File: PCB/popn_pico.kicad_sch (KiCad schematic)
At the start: 35 parts, among them SW1 KAN4542-0701C, SW2 KAN4542-0701C, U1 Pico

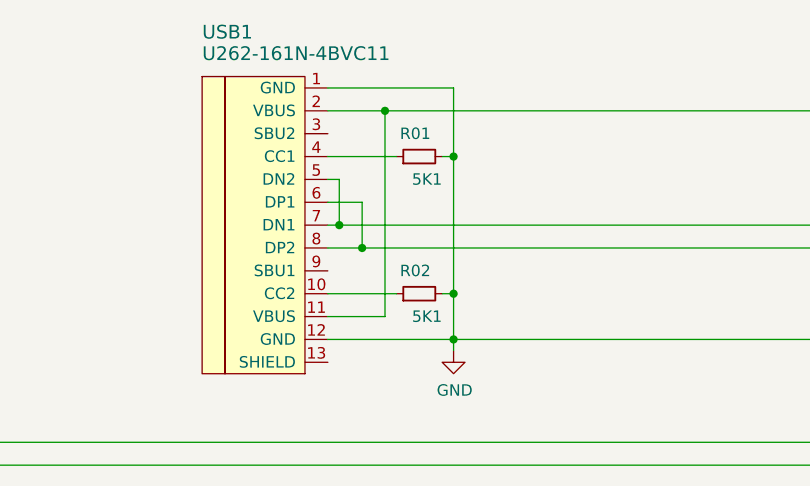
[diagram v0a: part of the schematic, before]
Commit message: Update PCB with libs and 3d models
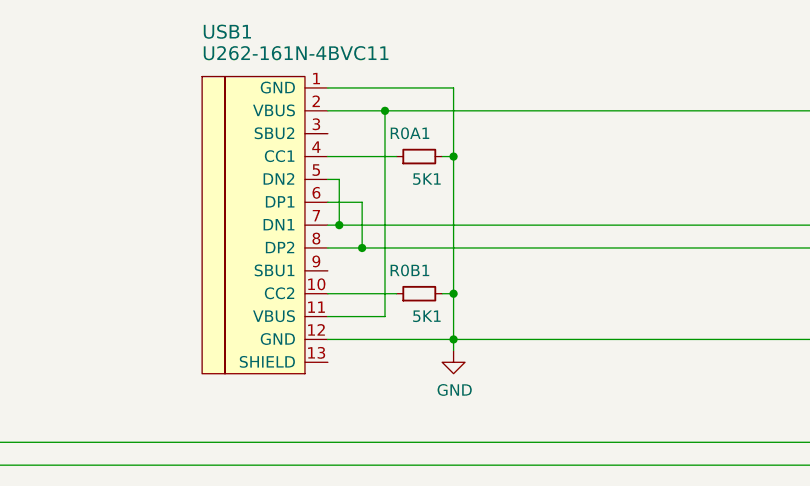
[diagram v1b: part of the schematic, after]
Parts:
- renumbered R01 to R0A1, R02 to R0B1
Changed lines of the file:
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@@
   (junction (at 199.39 142.24) (diameter 0) (color 0 0 0 0)
   )
+  (junction (at 259.08 106.68) (diameter 0) (color 0 0 0 0)
+  )
+  (junction (at 259.08 49.53) (diameter 0) (color 0 0 0 0)
+  )
+  (junction (at 95.25 180.34) (diameter 0) (color 0 0 0 0)
+  )
+  (junction (at 99.06 27.94) (diameter 0) (color 0 0 0 0)
+  )
+  (junction (at 262.89 74.93) (diameter 0) (color 0 0 0 0)
+  )
+  (junction (at 106.68 53.34) (diameter 0) (color 0 0 0 0)
+  )
+  (junction (at 262.89 109.22) (diameter 0) (color 0 0 0 0)
+  )
+  (junction (at 26.67 180.34) (diameter 0) (color 0 0 0 0)
+  )
+  (junction (at 259.08 129.54) (diameter 0) (color 0 0 0 0)
+  )
+  (junction (at 54.61 180.34) (diameter 0) (color 0 0 0 0)
+  )
+  (junction (at 179.07 153.67) (diameter 0) (color 0 0 0 0)
+  )
+  (junction (at 262.89 52.07) (diameter 0) (color 0 0 0 0)
+  )
+  (junction (at 43.18 156.21) (diameter 0) (color 0 0 0 0)
+  )
+  (junction (at 259.08 95.25) (diameter 0) (color 0 0 0 0)
+  )
+  (junction (at 140.97 171.45) (diameter 0) (color 0 0 0 0)
+  )
+  (junction (at 71.12 156.21) (diameter 0) (color 0 0 0 0)
+  )
+  (junction (at 259.08 140.97) (diameter 0) (color 0 0 0 0)
+  )
+  (junction (at 259.08 72.39) (diameter 0) (color 0 0 0 0)
+  )
+  (junction (at 259.08 118.11) (diameter 0) (color 0 0 0 0)
+  )
+  (junction (at 85.09 171.45) (diameter 0) (color 0 0 0 0)
+  )
   (junction (at 262.89 40.64) (diameter 0) (color 0 0 0 0)
   )
-  (junction (at 259.08 106.68) (diameter 0) (color 0 0 0 0)
-  )
-  (junction (at 259.08 49.53) (diameter 0) (color 0 0 0 0)
-  )
-  (junction (at 95.25 180.34) (diameter 0) (color 0 0 0 0)
-  )
-  (junction (at 99.06 27.94) (diameter 0) (color 0 0 0 0)
-  )
-  (junction (at 262.89 74.93) (diameter 0) (color 0 0 0 0)
-  )
-  (junction (at 106.68 53.34) (diameter 0) (color 0 0 0 0)
-  )
-  (junction (at 262.89 109.22) (diameter 0) (color 0 0 0 0)
-  )
-  (junction (at 26.67 180.34) (diameter 0) (color 0 0 0 0)
-  )
-  (junction (at 259.08 129.54) (diameter 0) (color 0 0 0 0)
-  )
-  (junction (at 54.61 180.34) (diameter 0) (color 0 0 0 0)
-  )
-  (junction (at 179.07 153.67) (diameter 0) (color 0 0 0 0)
-  )
-  (junction (at 262.89 52.07) (diameter 0) (color 0 0 0 0)
-  )
-  (junction (at 43.18 156.21) (diameter 0) (color 0 0 0 0)
-  )
-  (junction (at 259.08 95.25) (diameter 0) (color 0 0 0 0)
-  )
-  (junction (at 140.97 171.45) (diameter 0) (color 0 0 0 0)
-  )
-  (junction (at 71.12 156.21) (diameter 0) (color 0 0 0 0)
-  )
-  (junction (at 259.08 140.97) (diameter 0) (color 0 0 0 0)
-  )
-  (junction (at 259.08 118.11) (diameter 0) (color 0 0 0 0)
-  )
-  (junction (at 85.09 171.45) (diameter 0) (color 0 0 0 0)
-  )
   (junction (at 262.89 132.08) (diameter 0) (color 0 0 0 0)
   )
@@
   (junction (at 106.68 48.26) (diameter 0) (color 0 0 0 0)
   )
-  (junction (at 259.08 72.39) (diameter 0) (color 0 0 0 0)
-  )
   (junction (at 259.08 83.82) (diameter 0) (color 0 0 0 0)
   )
@@
     (stroke (width 0) (type default) (color 0 0 0 0))
   )
+  (wire (pts (xy 259.08 72.39) (xy 259.08 83.82))
+    (stroke (width 0) (type default) (color 0 0 0 0))
+  )
   (wire (pts (xy 236.22 132.08) (xy 236.22 140.97))
     (stroke (width 0) (type default) (color 0 0 0 0))
@@
     (stroke (width 0) (type default) (color 0 0 0 0))
   )
+  (wire (pts (xy 256.54 72.39) (xy 259.08 72.39))
+    (stroke (width 0) (type default) (color 0 0 0 0))
+  )
   (wire (pts (xy 119.38 105.41) (xy 119.38 133.35))
     (stroke (width 0) (type default) (color 0 0 0 0))
@@
     (stroke (width 0) (type default) (color 0 0 0 0))
   )
-  (wire (pts (xy 256.54 72.39) (xy 259.08 72.39))
-    (stroke (width 0) (type default) (color 0 0 0 0))
-  )
   (wire (pts (xy 46.99 153.67) (xy 50.8 153.67))
     (stroke (width 0) (type default) (color 0 0 0 0))
@@
     (stroke (width 0) (type default) (color 0 0 0 0))
   )
-  (wire (pts (xy 259.08 72.39) (xy 259.08 83.82))
+  (wire (pts (xy 259.08 60.96) (xy 259.08 72.39))
     (stroke (width 0) (type default) (color 0 0 0 0))
   )
@@
     (stroke (width 0) (type default) (color 0 0 0 0))
   )
-  (wire (pts (xy 259.08 60.96) (xy 259.08 72.39))
-    (stroke (width 0) (type default) (color 0 0 0 0))
-  )
   (wire (pts (xy 256.54 97.79) (xy 262.89 97.79))
     (stroke (width 0) (type default) (color 0 0 0 0))
@@
     (stroke (width 0) (type default) (color 0 0 0 0))
   )
+  (wire (pts (xy 256.54 40.64) (xy 262.89 40.64))
+    (stroke (width 0) (type default) (color 0 0 0 0))
+  )
   (wire (pts (xy 60.96 168.91) (xy 64.77 168.91))
     (stroke (width 0) (type default) (color 0 0 0 0))
@@
     (stroke (width 0) (type default) (color 0 0 0 0))
   )
+  (wire (pts (xy 262.89 40.64) (xy 262.89 52.07))
+    (stroke (width 0) (type default) (color 0 0 0 0))
+  )
   (wire (pts (xy 128.27 154.94) (xy 128.27 156.21))
     (stroke (width 0) (type default) (color 0 0 0 0))
@@
     (stroke (width 0) (type default) (color 0 0 0 0))
   )
-  (wire (pts (xy 262.89 40.64) (xy 262.89 52.07))
+  (wire (pts (xy 262.89 27.94) (xy 262.89 40.64))
     (stroke (width 0) (type default) (color 0 0 0 0))
   )
@@
     (stroke (width 0) (type default) (color 0 0 0 0))
   )
-  (wire (pts (xy 262.89 27.94) (xy 262.89 40.64))
-    (stroke (width 0) (type default) (color 0 0 0 0))
-  )
   (wire (pts (xy 205.74 128.27) (xy 179.07 128.27))
     (stroke (width 0) (type default) (color 0 0 0 0))
@@
   )
   (wire (pts (xy 198.12 85.09) (xy 208.28 85.09))
-    (stroke (width 0) (type default) (color 0 0 0 0))
-  )
-  (wire (pts (xy 256.54 40.64) (xy 262.89 40.64))
     (stroke (width 0) (type default) (color 0 0 0 0))
   )
@@
   (symbol (lib_id "Device:R_Small") (at 102.87 48.26 90) (unit 1)
     (in_bom yes) (on_board yes)
-    (property "Reference" "R02" (id 0) (at 104.14 45.72 90)
+    (property "Reference" "R0B1" (id 0) (at 104.14 45.72 90)
       (effects (font (size 1.27 1.27)) (justify left))
     )
@@
   (symbol (lib_id "Device:R_Small") (at 102.87 33.02 90) (unit 1)
     (in_bom yes) (on_board yes)
-    (property "Reference" "R01" (id 0) (at 104.14 30.48 90)
+    (property "Reference" "R0A1" (id 0) (at 104.14 30.48 90)
       (effects (font (size 1.27 1.27)) (justify left))
     )
@@
     )
     (path "/00000000-0000-0000-0000-000060fbdf0c"
-      (reference "R01") (unit 1) (value "5K1") (footprint "Resistor_SMD:R_0603_1608Metric")
+      (reference "R0A1") (unit 1) (value "5K1") (footprint "Resistor_SMD:R_0603_1608Metric")
+    )
+    (path "/00000000-0000-0000-0000-000060fbd2ca"
+      (reference "R0B1") (unit 1) (value "5K1") (footprint "Resistor_SMD:R_0603_1608Metric")
     )
     (path "/b5e174f6-ca34-4825-9b26-9b13f36373a8"
       (reference "R1") (unit 1) (value "220R") (footprint "Resistor_SMD:R_0603_1608Metric")
     )
-    (path "/00000000-0000-0000-0000-000060fbd2ca"
-      (reference "R02") (unit 1) (value "5K1") (footprint "Resistor_SMD:R_0603_1608Metric")
-    )
     (path "/eb72f3f9-3bba-47fb-bf5e-ecf59a99b837"

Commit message: Finished layout
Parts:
- MX1: value MX-LED-B -> MX-BUTTON; footprint MX_Only:MXOnly-1.5U-Hotswap-LED-SMD -> MX_Only:MXOnly-Popn_Button-Hotswap-LED
- MX2, MX3, MX4, MX5: value MX-LED -> MX-BUTTON; footprint MX_Only:MXOnly-1.5U-Hotswap-LED-SMD -> MX_Only:MXOnly-Popn_Button-Hotswap-LED
- MX6, MX7, MX8, MX9: value MX-LED-R -> MX-BUTTON; footprint MX_Only:MXOnly-1.5U-Hotswap-LED-SMD -> MX_Only:MXOnly-Popn_Button-Hotswap-LED
- U1: footprint MCU_RaspberryPi_and_Boards:RPi_Pico_SMD_TH -> MCU_RaspberryPi_and_Boards:RPi_Pico_SMD
- renumbered R0A1 to R20, R0B1 to R21
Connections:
- no-connect marks 0 -> 17
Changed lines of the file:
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@@
   (junction (at 224.79 107.95) (diameter 0) (color 0 0 0 0)
   )
+  (no_connect (at 92.71 55.88))
+  (no_connect (at 92.71 30.48))
+  (no_connect (at 92.71 45.72))
+  (no_connect (at 198.12 82.55))
+  (no_connect (at 198.12 90.17))
+  (no_connect (at 198.12 92.71))
+  (no_connect (at 198.12 97.79))
+  (no_connect (at 198.12 100.33))
+  (no_connect (at 198.12 102.87))
+  (no_connect (at 198.12 67.31))
+  (no_connect (at 198.12 72.39))
+  (no_connect (at 198.12 74.93))
+  (no_connect (at 198.12 77.47))
+  (no_connect (at 162.56 69.85))
+  (no_connect (at 162.56 82.55))
+  (no_connect (at 162.56 95.25))
+  (no_connect (at 162.56 107.95))
   (wire (pts (xy 62.23 77.47) (xy 162.56 77.47))
     (stroke (width 0) (type default) (color 0 0 0 0))
@@
       (effects (font (size 1.27 1.27)) (justify right))
     )
-    (property "Footprint" "MCU_RaspberryPi_and_Boards:RPi_Pico_SMD_TH" (id 2) (at 180.34 88.9 90)
+    (property "Footprint" "MCU_RaspberryPi_and_Boards:RPi_Pico_SMD" (id 2) (at 180.34 88.9 90)
       (effects (font (size 1.27 1.27)) hide)
     )
@@
       (effects (font (size 1.524 1.524)))
     )
-    (property "Value" "MX-LED-B" (id 1) (at 29.21 164.4396 0)
+    (property "Value" "MX-BUTTON" (id 1) (at 29.21 164.4396 0)
       (effects (font (size 0.508 0.508)))
     )
-    (property "Footprint" "MX_Only:MXOnly-1.5U-Hotswap-LED-SMD" (id 2) (at 14.605 168.275 0)
+    (property "Footprint" "MX_Only:MXOnly-Popn_Button-Hotswap-LED" (id 2) (at 14.605 168.275 0)
       (effects (font (size 1.524 1.524)) hide)
     )
@@
       (effects (font (size 1.524 1.524)))
     )
-    (property "Value" "MX-LED" (id 1) (at 43.18 149.1996 0)
+    (property "Value" "MX-BUTTON" (id 1) (at 43.18 149.1996 0)
       (effects (font (size 0.508 0.508)))
     )
-    (property "Footprint" "MX_Only:MXOnly-1.5U-Hotswap-LED-SMD" (id 2) (at 28.575 153.035 0)
+    (property "Footprint" "MX_Only:MXOnly-Popn_Button-Hotswap-LED" (id 2) (at 28.575 153.035 0)
       (effects (font (size 1.524 1.524)) hide)
     )
@@
       (effects (font (size 1.524 1.524)))
     )
-    (property "Value" "MX-LED" (id 1) (at 57.15 164.4396 0)
+    (property "Value" "MX-BUTTON" (id 1) (at 57.15 164.4396 0)
       (effects (font (size 0.508 0.508)))
     )
-    (property "Footprint" "MX_Only:MXOnly-1.5U-Hotswap-LED-SMD" (id 2) (at 42.545 168.275 0)
+    (property "Footprint" "MX_Only:MXOnly-Popn_Button-Hotswap-LED" (id 2) (at 42.545 168.275 0)
       (effects (font (size 1.524 1.524)) hide)
     )
@@
       (effects (font (size 1.524 1.524)))
     )
-    (property "Value" "MX-LED" (id 1) (at 71.12 149.1996 0)
+    (property "Value" "MX-BUTTON" (id 1) (at 71.12 149.1996 0)
       (effects (font (size 0.508 0.508)))
     )
-    (property "Footprint" "MX_Only:MXOnly-1.5U-Hotswap-LED-SMD" (id 2) (at 56.515 153.035 0)
+    (property "Footprint" "MX_Only:MXOnly-Popn_Button-Hotswap-LED" (id 2) (at 56.515 153.035 0)
       (effects (font (size 1.524 1.524)) hide)
     )
@@
       (effects (font (size 1.524 1.524)))
     )
-    (property "Value" "MX-LED" (id 1) (at 85.09 164.4396 0)
+    (property "Value" "MX-BUTTON" (id 1) (at 85.09 164.4396 0)
       (effects (font (size 0.508 0.508)))
     )
-    (property "Footprint" "MX_Only:MXOnly-1.5U-Hotswap-LED-SMD" (id 2) (at 70.485 168.275 0)
+    (property "Footprint" "MX_Only:MXOnly-Popn_Button-Hotswap-LED" (id 2) (at 70.485 168.275 0)
       (effects (font (size 1.524 1.524)) hide)
     )
@@
       (effects (font (size 1.524 1.524)))
     )
-    (property "Value" "MX-LED-R" (id 1) (at 97.79 149.1996 0)
+    (property "Value" "MX-BUTTON" (id 1) (at 97.79 149.1996 0)
       (effects (font (size 0.508 0.508)))
     )
-    (property "Footprint" "MX_Only:MXOnly-1.5U-Hotswap-LED-SMD" (id 2) (at 83.185 153.035 0)
+    (property "Footprint" "MX_Only:MXOnly-Popn_Button-Hotswap-LED" (id 2) (at 83.185 153.035 0)
       (effects (font (size 1.524 1.524)) hide)
     )
@@
       (effects (font (size 1.524 1.524)))
     )
-    (property "Value" "MX-LED-R" (id 1) (at 111.76 164.4396 0)
+    (property "Value" "MX-BUTTON" (id 1) (at 111.76 164.4396 0)
       (effects (font (size 0.508 0.508)))
     )
-    (property "Footprint" "MX_Only:MXOnly-1.5U-Hotswap-LED-SMD" (id 2) (at 97.155 168.275 0)
+    (property "Footprint" "MX_Only:MXOnly-Popn_Button-Hotswap-LED" (id 2) (at 97.155 168.275 0)
       (effects (font (size 1.524 1.524)) hide)
     )
@@
   (symbol (lib_id "Device:R_Small") (at 102.87 48.26 90) (unit 1)
     (in_bom yes) (on_board yes)
-    (property "Reference" "R0B1" (id 0) (at 104.14 45.72 90)
+    (property "Reference" "R21" (id 0) (at 104.14 45.72 90)
       (effects (font (size 1.27 1.27)) (justify left))
     )
@@
   (symbol (lib_id "Device:R_Small") (at 102.87 33.02 90) (unit 1)
     (in_bom yes) (on_board yes)
-    (property "Reference" "R0A1" (id 0) (at 104.14 30.48 90)
+    (property "Reference" "R20" (id 0) (at 104.14 30.48 90)
       (effects (font (size 1.27 1.27)) (justify left))
     )
@@
       (effects (font (size 1.524 1.524)))
     )
-    (property "Value" "MX-LED-R" (id 1) (at 140.97 164.4396 0)
+    (property "Value" "MX-BUTTON" (id 1) (at 140.97 164.4396 0)
       (effects (font (size 0.508 0.508)))
     )
-    (property "Footprint" "MX_Only:MXOnly-1.5U-Hotswap-LED-SMD" (id 2) (at 126.365 168.275 0)
+    (property "Footprint" "MX_Only:MXOnly-Popn_Button-Hotswap-LED" (id 2) (at 126.365 168.275 0)
       (effects (font (size 1.524 1.524)) hide)
     )
@@
       (effects (font (size 1.524 1.524)))
     )
-    (property "Value" "MX-LED-R" (id 1) (at 127 149.1996 0)
+    (property "Value" "MX-BUTTON" (id 1) (at 127 149.1996 0)
       (effects (font (size 0.508 0.508)))
     )
-    (property "Footprint" "MX_Only:MXOnly-1.5U-Hotswap-LED-SMD" (id 2) (at 112.395 153.035 0)
+    (property "Footprint" "MX_Only:MXOnly-Popn_Button-Hotswap-LED" (id 2) (at 112.395 153.035 0)
       (effects (font (size 1.524 1.524)) hide)
     )
@@
     )
     (path "/00000000-0000-0000-0000-000060e823b8"
-      (reference "MX1") (unit 1) (value "MX-LED-B") (footprint "MX_Only:MXOnly-1.5U-Hotswap-LED-SMD")
+      (reference "MX1") (unit 1) (value "MX-BUTTON") (footprint "MX_Only:MXOnly-Popn_Button-Hotswap-LED")
     )
     (path "/00000000-0000-0000-0000-000060e841d6"
-      (reference "MX2") (unit 1) (value "MX-LED") (footprint "MX_Only:MXOnly-1.5U-Hotswap-LED-SMD")
+      (reference "MX2") (unit 1) (value "MX-BUTTON") (footprint "MX_Only:MXOnly-Popn_Button-Hotswap-LED")
     )
     (path "/00000000-0000-0000-0000-000060e84ea8"
-      (reference "MX3") (unit 1) (value "MX-LED") (footprint "MX_Only:MXOnly-1.5U-Hotswap-LED-SMD")
+      (reference "MX3") (unit 1) (value "MX-BUTTON") (footprint "MX_Only:MXOnly-Popn_Button-Hotswap-LED")
     )
     (path "/00000000-0000-0000-0000-000060e85693"
-      (reference "MX4") (unit 1) (value "MX-LED") (footprint "MX_Only:MXOnly-1.5U-Hotswap-LED-SMD")
+      (reference "MX4") (unit 1) (value "MX-BUTTON") (footprint "MX_Only:MXOnly-Popn_Button-Hotswap-LED")
     )
     (path "/00000000-0000-0000-0000-000060e85fe6"
-      (reference "MX5") (unit 1) (value "MX-LED") (footprint "MX_Only:MXOnly-1.5U-Hotswap-LED-SMD")
+      (reference "MX5") (unit 1) (value "MX-BUTTON") (footprint "MX_Only:MXOnly-Popn_Button-Hotswap-LED")
     )
     (path "/00000000-0000-0000-0000-000060e866af"
-      (reference "MX6") (unit 1) (value "MX-LED-R") (footprint "MX_Only:MXOnly-1.5U-Hotswap-LED-SMD")
+      (reference "MX6") (unit 1) (value "MX-BUTTON") (footprint "MX_Only:MXOnly-Popn_Button-Hotswap-LED")
     )
     (path "/00000000-0000-0000-0000-000060e872a0"
-      (reference "MX7") (unit 1) (value "MX-LED-R") (footprint "MX_Only:MXOnly-1.5U-Hotswap-LED-SMD")
+      (reference "MX7") (unit 1) (value "MX-BUTTON") (footprint "MX_Only:MXOnly-Popn_Button-Hotswap-LED")
     )
     (path "/83dc4520-a0be-4060-9186-57920bcaeee2"
-      (reference "MX8") (unit 1) (value "MX-LED-R") (footprint "MX_Only:MXOnly-1.5U-Hotswap-LED-SMD")
+      (reference "MX8") (unit 1) (value "MX-BUTTON") (footprint "MX_Only:MXOnly-Popn_Button-Hotswap-LED")
     )
     (path "/34ec89be-a189-4954-9456-b25767ad1d07"
-      (reference "MX9") (unit 1) (value "MX-LED-R") (footprint "MX_Only:MXOnly-1.5U-Hotswap-LED-SMD")
-    )
-    (path "/00000000-0000-0000-0000-000060fbdf0c"
-      (reference "R0A1") (unit 1) (value "5K1") (footprint "Resistor_SMD:R_0603_1608Metric")
-    )
-    (path "/00000000-0000-0000-0000-000060fbd2ca"
-      (reference "R0B1") (unit 1) (value "5K1") (footprint "Resistor_SMD:R_0603_1608Metric")
+      (reference "MX9") (unit 1) (value "MX-BUTTON") (footprint "MX_Only:MXOnly-Popn_Button-Hotswap-LED")
     )
     (path "/b5e174f6-ca34-4825-9b26-9b13f36373a8"
@@
       (reference "R10") (unit 1) (value "220R") (footprint "Resistor_SMD:R_0603_1608Metric")
     )
+    (path "/00000000-0000-0000-0000-000060fbdf0c"
+      (reference "R20") (unit 1) (value "5K1") (footprint "Resistor_SMD:R_0603_1608Metric")
+    )
+    (path "/00000000-0000-0000-0000-000060fbd2ca"
+      (reference "R21") (unit 1) (value "5K1") (footprint "Resistor_SMD:R_0603_1608Metric")
+    )
     (path "/21b49463-8180-4913-bc8e-b5e454cca286"
       (reference "SW1") (unit 1) (value "KAN4542-0701C") (footprint "K2-1102SP-C4SC-04:KAN4542-0701C")
@@
     )
     (path "/00000000-0000-0000-0000-000060e7e781"
-      (reference "U1") (unit 1) (value "Pico") (footprint "MCU_RaspberryPi_and_Boards:RPi_Pico_SMD_TH")
+      (reference "U1") (unit 1) (value "Pico") (footprint "MCU_RaspberryPi_and_Boards:RPi_Pico_SMD")
     )
     (path "/00000000-0000-0000-0000-000060f9a7f0"
